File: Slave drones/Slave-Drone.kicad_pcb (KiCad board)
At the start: 4 copper layers, 32 x 32 mm, 46 parts, among them J1 Conn_01x02, J2 Conn_01x02, J3 Conn_01x02, J4 Conn_01x02, J5 USB_C_Receptacle_USB2.0_16P, J6 Conn_01x02, SW1 SW_Push, SW2 SW_Push, U1 MPU6500, U2 QMC5883L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

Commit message: I broke the pcb file, had to restart routing
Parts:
- removed G***: LOGO, LOGO
- removed REF** (x4): MountingHole_2.1mm, MountingHole:MountingHole_2.1mm
- C1, C3, D6, R1, R10, R11, R12, R13, R14, R16, R17, R2, R3, R4, R5, R6, R7, R8, R9, SW1, SW2, U4: moved to F.Cu
- U3: footprint footprint-JLC:BULETM-SMD_ESP32-S3-MINI-1-N8 -> ESP32-S3-MINI-1-N8:XCVR_ESP32-S3-MINI-1-N8
- moved C2 61.9 mm to (164.9, 90.5), turned to 0 degrees
- moved U4 61.0 mm to (165.4, 87.0), turned to 0 degrees
- moved SW1 60.6 mm to (151.4, 108.9), turned to 0 degrees
- moved J6 59.8 mm to (160.1, 79.7)
- moved C3 58.0 mm to (164.9, 93.0), turned to 0 degrees
- moved MOSFET2 57.6 mm to (160.5, 92.1)
- moved R11 55.7 mm to (146.7, 107.6)
- moved R8 55.0 mm to (143.8, 111.6), turned to 0 degrees
- moved R4 55.0 mm to (140.9, 113.6), turned to 0 degrees
- moved R14 54.6 mm to (164.0, 80.4), turned to 0 degrees
- moved R13 54.5 mm to (164.0, 78.4)
- moved SW2 54.3 mm to (151.4, 113.3), turned to 0 degrees
- moved MOSFET3 53.4 mm to (160.5, 97.1), turned to 0 degrees
- moved R5 52.6 mm to (140.9, 115.6), turned to 0 degrees
- moved R9 51.9 mm to (143.8, 113.6)
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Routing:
- net /Motor_Power: track 72.5 -> 0.00 mm, vias 4 -> 0
- net GND: track 42.5 -> 0.00 mm, vias 20 -> 0
- net /SDA: track 33.9 -> 0.00 mm, vias 5 -> 0
- net /SCL: track 32.0 -> 0.00 mm, vias 4 -> 0
- net /Motor3: track 27.7 -> 0.00 mm, vias 2 -> 0
- net Net-(D5-A): track 25.9 -> 0.00 mm, vias 1 -> 0
- net +3.3V: track 24.4 -> 0.00 mm, vias 8 -> 0
- net Net-(U3-IO2): track 18.4 -> 0.00 mm, vias 2 -> 0
- net Net-(U3-IO4): track 18.1 -> 0.00 mm, vias 2 -> 0
- net /USBPWR: track 17.4 -> 0.00 mm, vias 1 -> 0
- net /USB_D+: track 14.0 -> 0.00 mm
- net /USB_D-: track 13.6 -> 0.00 mm
- net Net-(U3-IO1): track 10.7 -> 0.00 mm, vias 2 -> 0
- net /RESET: track 9.70 -> 0.00 mm, vias 1 -> 0
- net Net-(D3-A): track 8.35 -> 0.00 mm
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- removed copper zone on In2.Cu, net +3.3V
- removed copper zone on F.Cu, net GND
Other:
- board size 32 x 32 mm -> 48.1 x 44.6 mm
- copper layers 4 -> 2

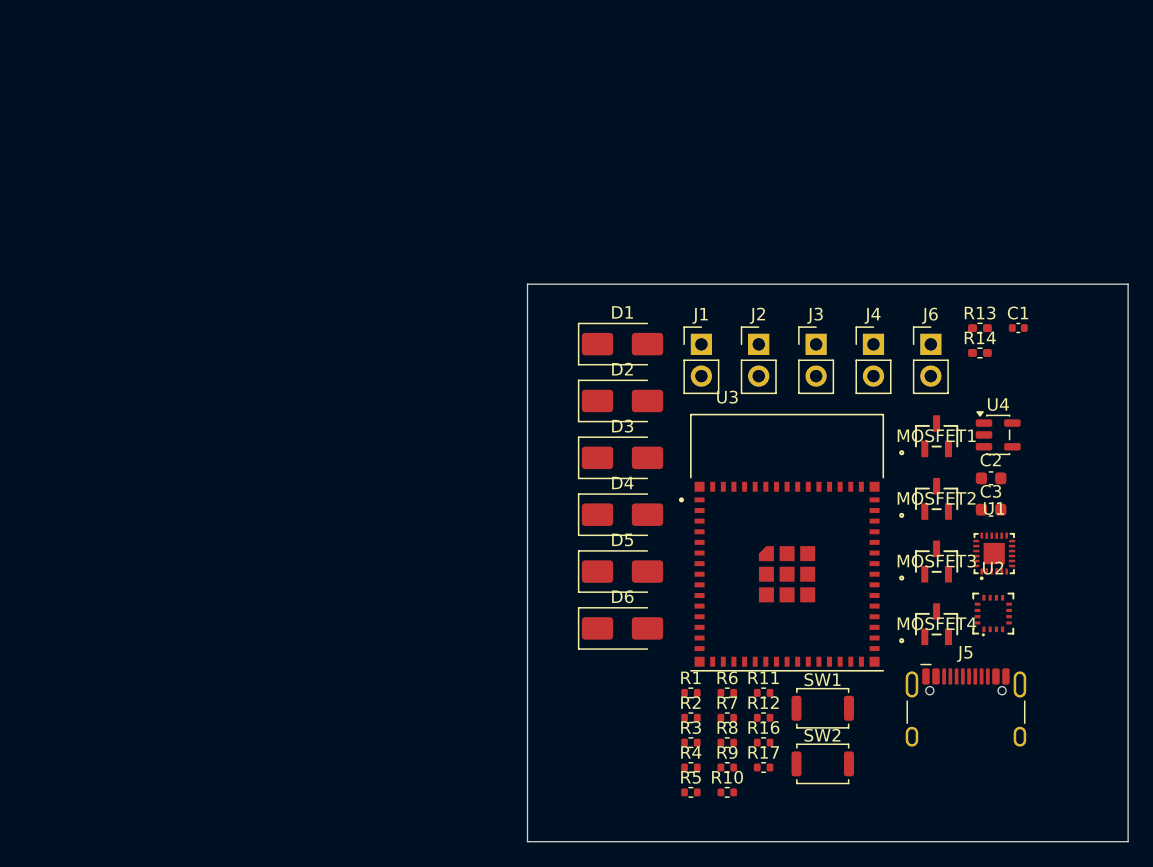
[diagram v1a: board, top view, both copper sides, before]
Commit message: tried fixing error 3 - failed - use work around
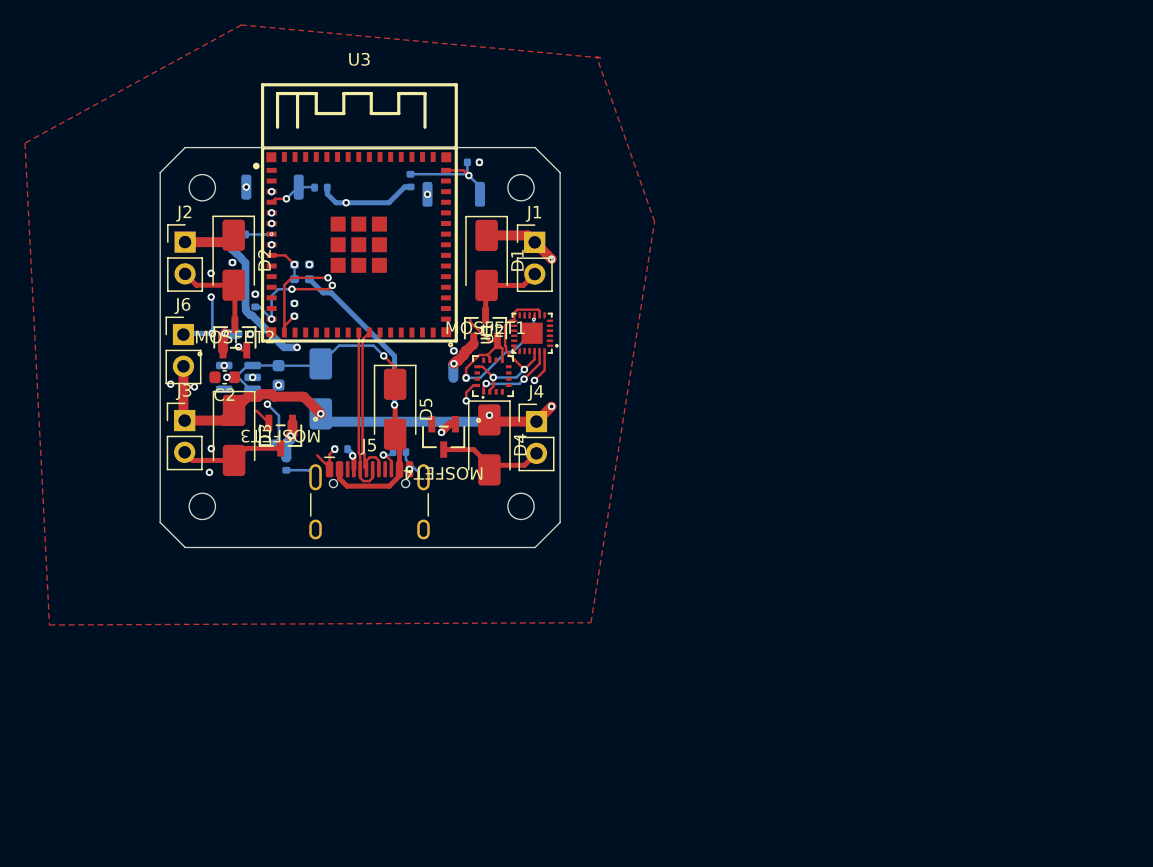
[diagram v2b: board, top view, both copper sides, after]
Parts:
- added G***: LOGO, LOGO, B.Cu at (121.4, 79.7)
- added REF**: MountingHole_2.1mm, MountingHole:MountingHole_2.1mm, B.Cu at (127.3, 67.2)
- added REF**: MountingHole_2.1mm, MountingHole:MountingHole_2.1mm, B.Cu at (101.8, 92.7)
- added REF**: MountingHole_2.1mm, MountingHole:MountingHole_2.1mm, B.Cu at (127.3, 92.7)
- added REF**: MountingHole_2.1mm, MountingHole:MountingHole_2.1mm, B.Cu at (101.8, 67.2)
- C1, C3, D6, R1, R10, R11, R12, R13, R14, R16, R17, R2, R3, R4, R5, R6, R7, R8, R9, SW1, SW2, U4: moved to B.Cu
- U3: footprint ESP32-S3-MINI-1-N8:XCVR_ESP32-S3-MINI-1-N8 -> footprint-JLC:BULETM-SMD_ESP32-S3-MINI-1-N8
- moved C2 61.9 mm to (103.5, 82.4), turned to 180 degrees
- moved U4 61.0 mm to (104.7, 82.4), turned to 180 degrees
- moved SW1 60.6 mm to (107.4, 67.2), turned to 180 degrees
- moved J6 59.8 mm to (100.2, 79.0)
- moved C3 58.0 mm to (107.9, 82.2), turned to -90 degrees
- moved MOSFET2 57.6 mm to (104.4, 79.2)
- moved R11 55.7 mm to (104.7, 71.0)
- moved R8 55.0 mm to (111.2, 67.2), turned to 180 degrees
- moved R4 55.0 mm to (104.2, 72.7), turned to -90 degrees
- moved R14 54.6 mm to (109.7, 74.5), turned to 180 degrees
- moved R13 54.5 mm to (109.7, 73.4)
- moved SW2 54.3 mm to (121.9, 67.7), turned to 180 degrees
- moved MOSFET3 53.4 mm to (108.0, 87.0), turned to 180 degrees
- moved R5 52.6 mm to (106.0, 76.2), turned to -90 degrees
- moved R9 51.9 mm to (105.1, 78.9)
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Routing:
- net /Motor_Power: track 0.00 -> 72.5 mm, vias 0 -> 4
- net GND: track 0.00 -> 42.5 mm, vias 0 -> 20
- net /SDA: track 0.00 -> 33.9 mm, vias 0 -> 5
- net /SCL: track 0.00 -> 32.0 mm, vias 0 -> 4
- net /Motor3: track 0.00 -> 27.7 mm, vias 0 -> 2
- net Net-(D5-A): track 0.00 -> 25.9 mm, vias 0 -> 1
- net +3.3V: track 0.00 -> 24.4 mm, vias 0 -> 8
- net Net-(U3-IO2): track 0.00 -> 18.4 mm, vias 0 -> 2
- net Net-(U3-IO4): track 0.00 -> 18.1 mm, vias 0 -> 2
- net /USBPWR: track 0.00 -> 17.4 mm, vias 0 -> 1
- net /USB_D+: track 0.00 -> 14.0 mm
- net /USB_D-: track 0.00 -> 13.6 mm
- net Net-(U3-IO1): track 0.00 -> 10.7 mm, vias 0 -> 2
- net /RESET: track 0.00 -> 9.70 mm, vias 0 -> 1
- net Net-(D3-A): track 0.00 -> 8.35 mm
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- added copper zone on In2.Cu, net +3.3V
- added copper zone on F.Cu, net GND
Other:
- board size 48.1 x 44.6 mm -> 32 x 32 mm
- copper layers 2 -> 4

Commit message: corrected mosfet placement
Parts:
- added R4: 10K, Resistor_SMD:R_0402_1005Metric, B.Cu at (122.3, 82.4)
- moved R1 19.2 mm to (104.0, 76.9), turned to 180 degrees
- moved MOSFET1 15.2 mm to (122.7, 93.6)
- moved MOSFET4 9.17 mm to (124.4, 78.6), turned to 0 degrees
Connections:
- MOSFET1 pad 1: /Motor4 -> /Motor3
- MOSFET1 pad 2: GND -> Net-(D4-A)
- MOSFET1 pad 3: Net-(D1-A) -> GND
- MOSFET2 pad 2: GND -> Net-(D2-A)
- MOSFET2 pad 3: Net-(D2-A) -> GND
- MOSFET3 pad 2: GND -> Net-(D3-A)
- MOSFET3 pad 3: Net-(D3-A) -> GND
- MOSFET4 pad 1: /Motor3 -> /Motor4
- MOSFET4 pad 2: GND -> Net-(D1-A)
- MOSFET4 pad 3: Net-(D4-A) -> GND
- R1 pad 1: /Motor4 -> /Motor3
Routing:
- net /Motor3: track 27.7 -> 35.2 mm
- net Net-(D2-A): track 7.47 -> 10.3 mm
- net GND: track 42.5 -> 39.7 mm
- net Net-(D1-A): track 6.88 -> 9.58 mm
- net Net-(D4-A): track 8.34 -> 9.44 mm
- net Net-(D3-A): track 8.35 -> 9.09 mm

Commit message: nothing
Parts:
- removed the R4 at (122.3, 82.4)
- moved R1 19.2 mm to (122.4, 82.4), turned to 0 degrees
- moved MOSFET1 15.2 mm to (124.4, 78.5)
- moved MOSFET4 9.17 mm to (121.1, 87.2), turned to 180 degrees
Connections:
- MOSFET1 pad 1: /Motor3 -> /Motor4
- MOSFET1 pad 2: Net-(D4-A) -> GND
- MOSFET1 pad 3: GND -> Net-(D1-A)
- MOSFET2 pad 2: Net-(D2-A) -> GND
- MOSFET2 pad 3: GND -> Net-(D2-A)
- MOSFET3 pad 2: Net-(D3-A) -> GND
- MOSFET3 pad 3: GND -> Net-(D3-A)
- MOSFET4 pad 1: /Motor4 -> /Motor3
- MOSFET4 pad 2: Net-(D1-A) -> GND
- MOSFET4 pad 3: GND -> Net-(D4-A)
- R1 pad 1: /Motor3 -> /Motor4
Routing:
- net /Motor3: track 35.2 -> 27.7 mm
- net Net-(D2-A): track 10.3 -> 7.47 mm
- net GND: track 39.7 -> 42.5 mm
- net Net-(D1-A): track 9.58 -> 6.88 mm
- net Net-(D4-A): track 9.44 -> 8.34 mm
- net Net-(D3-A): track 9.09 -> 8.35 mm
